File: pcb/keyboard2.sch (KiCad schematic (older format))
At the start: 20 parts, among them J1 usb_pcb, J2 CONN_01X09, U1 atmega8u2-qfn, X1 resonator

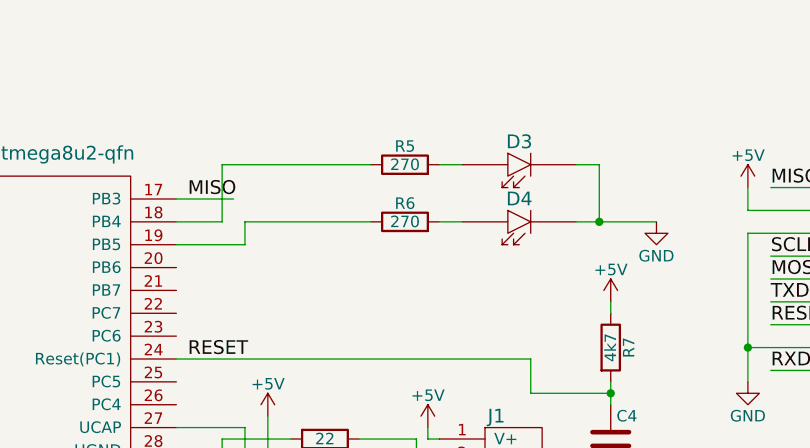
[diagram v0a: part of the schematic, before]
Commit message: Edit resistor value.
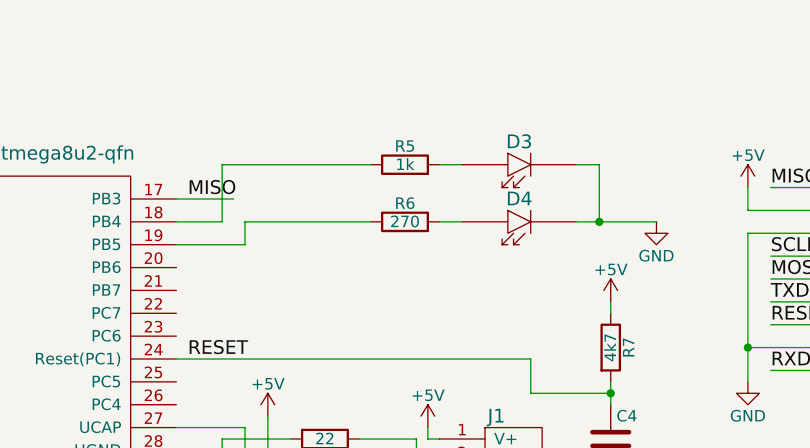
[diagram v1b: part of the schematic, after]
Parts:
- R5: value 270 -> 1k; DigikeyPart 311-270LRCT-ND -> 311-1KLBCT-ND
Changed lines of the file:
@@
 P 7150 2200
 F 0 "R5" V 7230 2200 50  0000 C CNN
-F 1 "270" V 7150 2200 50  0000 C CNN
+F 1 "1k" V 7150 2200 50  0000 C CNN
 F 2 "oscu_footprints:R_0402_nosilk" V 7080 2200 30  0001 C CNN
 F 3 "" H 7150 2200 30  0000 C CNN
-F 4 "311-270LRCT-ND" V 7150 2200 60  0001 C CNN "DigikeyPart"
+F 4 "311-1KLBCT-ND" V 7150 2200 60  0001 C CNN "DigikeyPart"
 	1    7150 2200
 	0    -1   -1   0

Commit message: Schematic part changes.
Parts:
- D1: value led1 -> led_red
- D2: value led1 -> led_green
- D3: value led1 -> led_blue
- D4: value led1 -> led_yellow
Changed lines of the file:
@@
 P 2850 3100
 F 0 "D1" H 2850 3200 60  0000 C CNN
-F 1 "led1" H 2850 3000 60  0001 C CNN
+F 1 "led_red" H 2850 3000 60  0001 C CNN
 F 2 "oscu_footprints:LED_0603_nosilk" H 2850 3100 60  0001 C CNN
 F 3 "" H 2850 3100 60  0000 C CNN
@@
 P 2850 2850
 F 0 "D2" H 2850 2950 60  0000 C CNN
-F 1 "led1" H 2850 2750 60  0001 C CNN
+F 1 "led_green" H 2850 2750 60  0001 C CNN
 F 2 "oscu_footprints:LED_0603_nosilk" H 2850 2850 60  0001 C CNN
 F 3 "" H 2850 2850 60  0000 C CNN
@@
 P 7650 2200
 F 0 "D3" H 7650 2300 60  0000 C CNN
-F 1 "led1" H 7650 2100 60  0001 C CNN
+F 1 "led_blue" H 7650 2100 60  0001 C CNN
 F 2 "oscu_footprints:LED_0603_nosilk" H 7650 2200 60  0001 C CNN
 F 3 "" H 7650 2200 60  0000 C CNN
@@
 P 7650 2450
 F 0 "D4" H 7650 2550 60  0000 C CNN
-F 1 "led1" H 7650 2350 60  0001 C CNN
+F 1 "led_yellow" H 7650 2350 60  0001 C CNN
 F 2 "oscu_footprints:LED_0603_nosilk" H 7650 2450 60  0001 C CNN
 F 3 "" H 7650 2450 60  0000 C CNN

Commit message: added and updated libraries
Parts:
- B1: footprint oscu_footprints:button_smd_panasonic -> keyboard2_footprints:button_smd_panasonic
- C1, C2, C3, C4: footprint oscu_footprints:C_0402_nosilk -> keyboard2_footprints:C_0402_nosilk
- D1, D2, D3, D4: footprint oscu_footprints:LED_0603_nosilk -> keyboard2_footprints:LED_0603_nosilk
- J1: footprint oscu_footprints:usb_pcb -> keyboard2_footprints:usb_pcb
- J2: footprint oscu_footprints:connector_smd_round2 -> keyboard2_footprints:connector_smd_round2
- R1, R2, R3, R4, R5, R6, R7: footprint oscu_footprints:R_0402_nosilk -> keyboard2_footprints:R_0402_nosilk
- U1: footprint oscu_footprints:qfn32_nosilk -> keyboard2_footprints:qfn32_nosilk
- X1: footprint oscu_footprints:resonator_murata_smd -> keyboard2_footprints:resonator_murata_smd
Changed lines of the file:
@@
 LIBS:memory
 LIBS:xilinx
-LIBS:special
 LIBS:microcontrollers
 LIBS:dsp
@@
 LIBS:contrib
 LIBS:valves
-LIBS:oscu_kicad_lib
 LIBS:keyboard2-cache
 EELAYER 25 0
@@
 F 0 "X1" H 4150 2350 60  0000 C CNN
 F 1 "resonator" H 4150 1800 60  0001 C CNN
-F 2 "oscu_footprints:resonator_murata_smd" H 4150 2200 60  0001 C CNN
+F 2 "keyboard2_footprints:resonator_murata_smd" H 4150 2200 60  0001 C CNN
 F 3 "" H 4150 2200 60  0000 C CNN
 F 4 "490-1219-1-ND" H 4150 2200 60  0001 C CNN "DigikeyPart"
@@
 F 0 "U1" H 4950 4050 60  0000 C CNN
 F 1 "atmega8u2-qfn" H 5650 4050 60  0000 C CNN
-F 2 "oscu_footprints:qfn32_nosilk" H 4850 4950 60  0001 C CNN
+F 2 "keyboard2_footprints:qfn32_nosilk" H 4850 4950 60  0001 C CNN
 F 3 "" H 4850 4950 60  0000 C CNN
 F 4 "ATMEGA32U2-MURCT" H 4850 3100 60  0001 C CNN "DigikeyPart"
@@
 F 0 "J1" H 7550 3800 60  0000 C CNN
 F 1 "usb_pcb" H 7700 3300 60  0000 C CNN
-F 2 "oscu_footprints:usb_pcb" H 7500 3550 60  0001 C CNN
+F 2 "keyboard2_footprints:usb_pcb" H 7500 3550 60  0001 C CNN
 F 3 "" H 7500 3550 60  0000 C CNN
 	1    7500 3550
@@
 F 0 "R1" V 6880 3400 50  0000 C CNN
 F 1 "22" V 6800 3400 50  0000 C CNN
-F 2 "oscu_footprints:R_0402_nosilk" V 6730 3400 30  0001 C CNN
+F 2 "keyboard2_footprints:R_0402_nosilk" V 6730 3400 30  0001 C CNN
 F 3 "" H 6800 3400 30  0000 C CNN
 F 4 "311-22.0LRCT-ND" V 6800 3400 60  0001 C CNN "DigikeyPart"
@@
 F 0 "R2" V 6880 3650 50  0000 C CNN
 F 1 "22" V 6800 3650 50  0000 C CNN
-F 2 "oscu_footprints:R_0402_nosilk" V 6730 3650 30  0001 C CNN
+F 2 "keyboard2_footprints:R_0402_nosilk" V 6730 3650 30  0001 C CNN
 F 3 "" H 6800 3650 30  0000 C CNN
 F 4 "311-22.0LRCT-ND" V 6800 3650 60  0001 C CNN "DigikeyPart"
@@
 F 0 "D1" H 2850 3200 60  0000 C CNN
 F 1 "led_red" H 2850 3000 60  0001 C CNN
-F 2 "oscu_footprints:LED_0603_nosilk" H 2850 3100 60  0001 C CNN
+F 2 "keyboard2_footprints:LED_0603_nosilk" H 2850 3100 60  0001 C CNN
 F 3 "" H 2850 3100 60  0000 C CNN
 F 4 "160-1446-1-ND" H 2850 3100 60  0001 C CNN "DigikeyPart"
@@
 F 0 "D2" H 2850 2950 60  0000 C CNN
 F 1 "led_green" H 2850 2750 60  0001 C CNN
-F 2 "oscu_footprints:LED_0603_nosilk" H 2850 2850 60  0001 C CNN
+F 2 "keyboard2_footprints:LED_0603_nosilk" H 2850 2850 60  0001 C CNN
 F 3 "" H 2850 2850 60  0000 C CNN
 F 4 "160-1447-1-ND" H 2850 2850 60  0001 C CNN "DigikeyPart"
@@
 F 0 "D3" H 7650 2300 60  0000 C CNN
 F 1 "led_blue" H 7650 2100 60  0001 C CNN
-F 2 "oscu_footprints:LED_0603_nosilk" H 7650 2200 60  0001 C CNN
+F 2 "keyboard2_footprints:LED_0603_nosilk" H 7650 2200 60  0001 C CNN
 F 3 "" H 7650 2200 60  0000 C CNN
 F 4 "160-1448-1-ND" H 7650 2200 60  0001 C CNN "DigikeyPart"
@@
 F 0 "D4" H 7650 2550 60  0000 C CNN
 F 1 "led_yellow" H 7650 2350 60  0001 C CNN
-F 2 "oscu_footprints:LED_0603_nosilk" H 7650 2450 60  0001 C CNN
+F 2 "keyboard2_footprints:LED_0603_nosilk" H 7650 2450 60  0001 C CNN
 F 3 "" H 7650 2450 60  0000 C CNN
 F 4 "160-1647-1-ND" H 7650 2450 60  0001 C CNN "DigikeyPart"
@@
 F 0 "B1" H 3250 4100 60  0000 C CNN
 F 1 "btn_sp2" H 3250 3850 60  0001 C CNN
-F 2 "oscu_footprints:button_smd_panasonic" H 3250 3950 60  0001 C CNN
+F 2 "keyboard2_footprints:button_smd_panasonic" H 3250 3950 60  0001 C CNN
 F 3 "" H 3250 3950 60  0000 C CNN
 F 4 "P8045SCT-ND" H 3250 3950 60  0001 C CNN "DigikeyPart"
@@
 F 0 "R3" V 3430 3100 50  0000 C CNN
 F 1 "270" V 3350 3100 50  0000 C CNN
-F 2 "oscu_footprints:R_0402_nosilk" V 3280 3100 30  0001 C CNN
+F 2 "keyboard2_footprints:R_0402_nosilk" V 3280 3100 30  0001 C CNN
 F 3 "" H 3350 3100 30  0000 C CNN
 F 4 "311-270LRCT-ND" V 3350 3100 60  0001 C CNN "DigikeyPart"
@@
 F 0 "R4" V 3430 2850 50  0000 C CNN
 F 1 "270" V 3350 2850 50  0000 C CNN
-F 2 "oscu_footprints:R_0402_nosilk" V 3280 2850 30  0001 C CNN
+F 2 "keyboard2_footprints:R_0402_nosilk" V 3280 2850 30  0001 C CNN
 F 3 "" H 3350 2850 30  0000 C CNN
 F 4 "311-270LRCT-ND" V 3350 2850 60  0001 C CNN "DigikeyPart"
@@
 F 0 "R5" V 7230 2200 50  0000 C CNN
 F 1 "1k" V 7150 2200 50  0000 C CNN
-F 2 "oscu_footprints:R_0402_nosilk" V 7080 2200 30  0001 C CNN
+F 2 "keyboard2_footprints:R_0402_nosilk" V 7080 2200 30  0001 C CNN
 F 3 "" H 7150 2200 30  0000 C CNN
 F 4 "311-1KLBCT-ND" V 7150 2200 60  0001 C CNN "DigikeyPart"
@@
 F 0 "R6" V 7230 2450 50  0000 C CNN
 F 1 "270" V 7150 2450 50  0000 C CNN
-F 2 "oscu_footprints:R_0402_nosilk" V 7080 2450 30  0001 C CNN
+F 2 "keyboard2_footprints:R_0402_nosilk" V 7080 2450 30  0001 C CNN
 F 3 "" H 7150 2450 30  0000 C CNN
 F 4 "311-270LRCT-ND" V 7150 2450 60  0001 C CNN "DigikeyPart"
@@
 F 0 "J2" H 9200 3200 50  0000 C CNN
 F 1 "CONN_01X09" V 9300 2700 50  0000 C CNN
-F 2 "oscu_footprints:connector_smd_round2" H 9200 2700 60  0001 C CNN
+F 2 "keyboard2_footprints:connector_smd_round2" H 9200 2700 60  0001 C CNN
 F 3 "" H 9200 2700 60  0000 C CNN
 	1    9200 2700
@@
 F 0 "C1" H 6475 4300 50  0000 L CNN
 F 1 "1u" H 6475 4100 50  0000 L CNN
-F 2 "oscu_footprints:C_0402_nosilk" H 6488 4050 30  0001 C CNN
+F 2 "keyboard2_footprints:C_0402_nosilk" H 6488 4050 30  0001 C CNN
 F 3 "" H 6450 4200 60  0000 C CNN
 F 4 "311-1702-1-ND" H 6450 4200 60  0001 C CNN "DigikeyPart"
@@
 F 0 "C2" H 6775 4300 50  0000 L CNN
 F 1 "1u" H 6775 4100 50  0000 L CNN
-F 2 "oscu_footprints:C_0402_nosilk" H 6788 4050 30  0001 C CNN
+F 2 "keyboard2_footprints:C_0402_nosilk" H 6788 4050 30  0001 C CNN
 F 3 "" H 6750 4200 60  0000 C CNN
 F 4 "311-1702-1-ND" H 6750 4200 60  0001 C CNN "DigikeyPart"
@@
 F 0 "C3" H 3525 2550 50  0000 L CNN
 F 1 "1u" H 3525 2350 50  0000 L CNN
-F 2 "oscu_footprints:C_0402_nosilk" H 3538 2300 30  0001 C CNN
+F 2 "keyboard2_footprints:C_0402_nosilk" H 3538 2300 30  0001 C CNN
 F 3 "" H 3500 2450 60  0000 C CNN
 F 4 "311-1702-1-ND" H 3500 2450 60  0001 C CNN "DigikeyPart"
@@
 F 0 "C4" H 8075 3500 50  0000 L CNN
 F 1 "100n" H 8075 3300 50  0000 L CNN
-F 2 "oscu_footprints:C_0402_nosilk" H 8088 3250 30  0001 C CNN
+F 2 "keyboard2_footprints:C_0402_nosilk" H 8088 3250 30  0001 C CNN
 F 3 "" H 8050 3400 60  0000 C CNN
 F 4 "311-1335-1-ND" H 8050 3400 60  0001 C CNN "DigikeyPart"
@@
 F 0 "R7" V 8130 3000 50  0000 C CNN
 F 1 "4k7" V 8050 3000 50  0000 C CNN
-F 2 "oscu_footprints:R_0402_nosilk" V 7980 3000 30  0001 C CNN
+F 2 "keyboard2_footprints:R_0402_nosilk" V 7980 3000 30  0001 C CNN
 F 3 "" H 8050 3000 30  0000 C CNN
 F 4 "311-4.7KLRCT-ND" V 8050 3000 60  0001 C CNN "DigikeyPart"

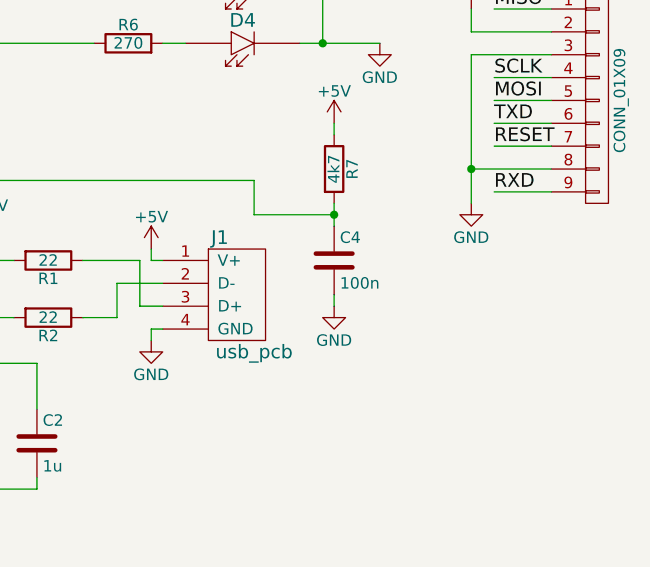
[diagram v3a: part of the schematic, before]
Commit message: update reset capacitor not mounted
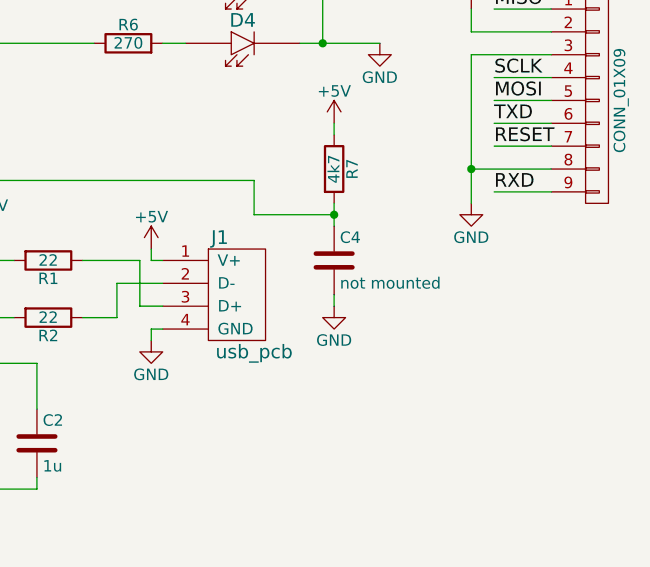
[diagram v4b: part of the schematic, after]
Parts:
- C4: value 100n -> not mounted
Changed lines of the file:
@@
 LIBS:contrib
 LIBS:valves
-LIBS:keyboard2-cache
+LIBS:keyboard2
 EELAYER 25 0
 EELAYER END
@@
 P 8050 3400
 F 0 "C4" H 8075 3500 50  0000 L CNN
-F 1 "100n" H 8075 3300 50  0000 L CNN
+F 1 "not mounted" H 8075 3300 50  0000 L CNN
 F 2 "keyboard2_footprints:C_0402_nosilk" H 8088 3250 30  0001 C CNN
 F 3 "" H 8050 3400 60  0000 C CNN
